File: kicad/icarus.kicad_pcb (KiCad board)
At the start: 4 copper layers, 64.7 x 44.2 mm, 80 parts, among them J1 CAN Bus, J2 CAN Bus, J3 SWD Programming, J4 USB_B_Micro, U1 MAX15062A, U10 XT30, U11 XT30, U12 XT30, U13 LT1787HVIMS8PBF, U14 USBLC6-2SC6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

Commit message: Added gerber and assembly files
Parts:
- added G***: LOGO, icarus_kicad_lib:Icarus_Logo, B.Cu at (147.8, 102.2)
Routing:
- net VSENSE_LOW: vias 0 -> 10
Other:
- board text added: "Jeremy Kanovsky Spring 2021"

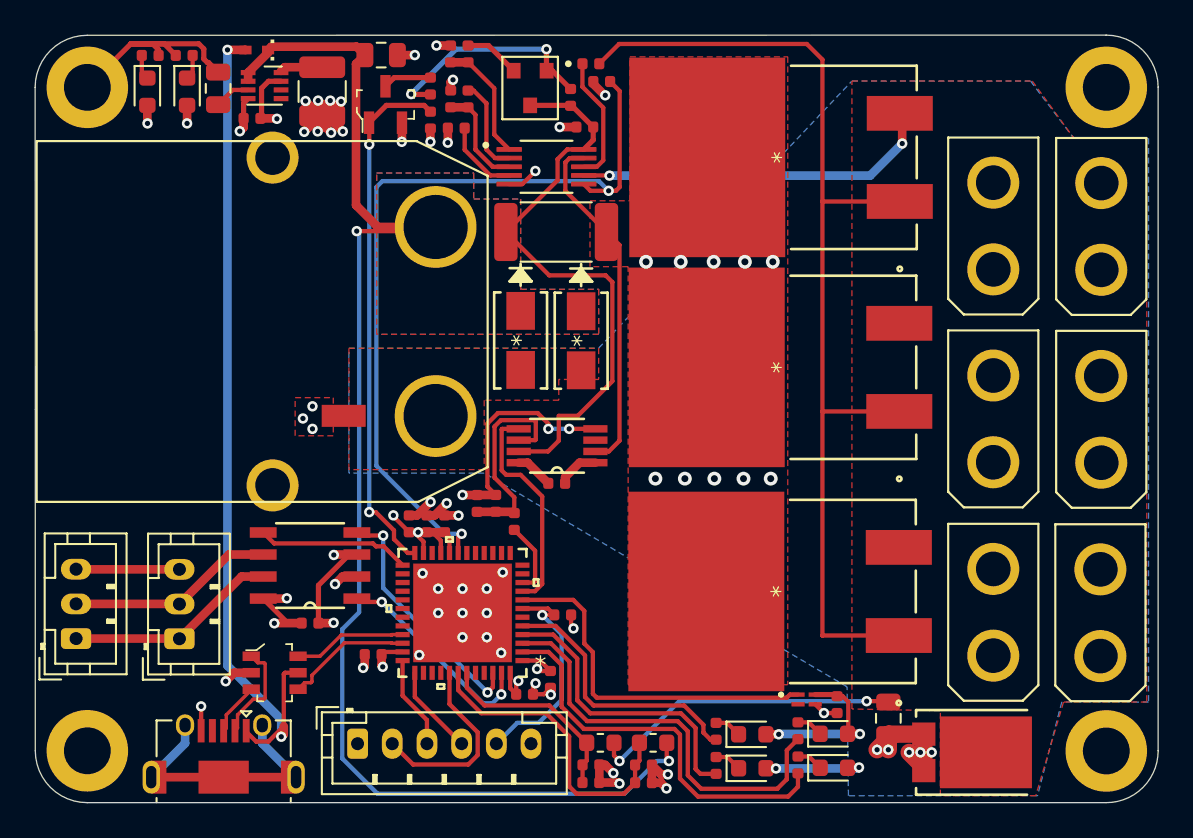
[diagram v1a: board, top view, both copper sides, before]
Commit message: Changed MCU due to sourcing problems
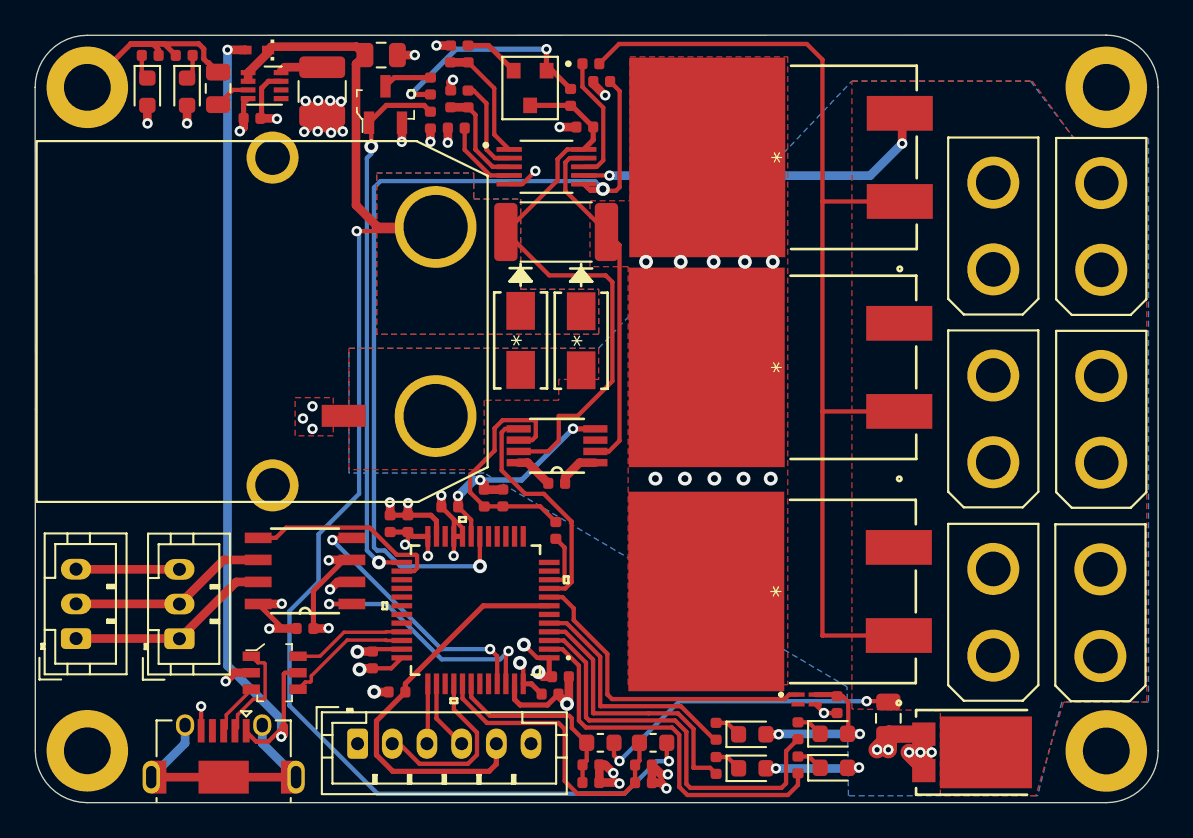
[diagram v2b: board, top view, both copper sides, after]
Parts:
- U2: value STM32G474CEU6 -> STM32G474CET6; footprint icarus_kicad_lib:STM32G474CEU6 -> icarus_kicad_lib:STM32G474CET6
- moved C5 10.5 mm to (133.6, 118.0), turned to 180 degrees
- moved R17 2.45 mm to (142.7, 108.7)
- moved C13 1.47 mm to (142.4, 118.1)
- moved C10 1.10 mm to (134.2, 108.3)
- moved C11 1.10 mm to (133.2, 108.3)
- moved C8 1.02 mm to (136.6, 107.3), turned to 0 degrees
- moved U2 0.77 mm to (138.1, 113.3)
- moved C9 0.60 mm to (143.0, 117.1), turned to 0 degrees
- moved C16 0.51 mm to (139.7, 106.8)
- moved R18 0.51 mm to (138.6, 106.8)
- moved G*** 0.46 mm to (148.0, 101.8)
- moved C1 0.42 mm to (128.3, 114.4)
- moved U3 0.42 mm to (128.3, 111.0)
- moved C12 0.31 mm to (132.2, 116.2), turned to 90 degrees
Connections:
- U2 pad 18: Net-(U2-Pad18) -> PG
- U2 pad 19: PG -> GND
- U2 pad 23: +3V3 -> GND
- U2 pad 24: TPS_ENABLE -> +3V3
- U2 pad 25: CAN_SHDN -> TPS_ENABLE
- U2 pad 26: Net-(U2-Pad26) -> CAN_SHDN
- U2 pad 35: +3V3 -> GND
- U2 pad 36: SWDIO -> +3V3
- U2 pad 37: SWCLK -> SWDIO
- U2 pad 38: Net-(U2-Pad38) -> SWCLK
- U2 pad 40: Net-(U2-Pad40) -> SWO
- U2 pad 41: SWO -> 24V_SENSE
- U2 pad 42: 24V_SENSE -> VSW_SENSE
- U2 pad 43: VSW_SENSE -> Net-(U2-Pad43)
- U2 pad 45: Net-(U2-Pad45) -> CAN_RX
- U2 pad 46: CAN_RX -> CAN_TX
- U2 pad 47: CAN_TX -> GND
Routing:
- net NRST: track 12.8 -> 23.6 mm, vias 1 -> 0
- net PG: track 46.2 -> 52.4 mm
- net GND: track 73.6 -> 79.3 mm, vias 44 -> 30
- net +3V3: track 53.6 -> 58.4 mm, vias 23 -> 26
- net CAN_SHDN: track 8.82 -> 11.7 mm
- net CAN_TX: track 12.3 -> 15.1 mm
- net VSENSE_HIGH: track 112.9 -> 115.5 mm
- net Net-(C16-Pad1): track 12.2 -> 14.5 mm
- net MOSFET_TEMP: track 20.8 -> 18.7 mm
- net SWDIO: track 5.37 -> 3.47 mm
- net LED4: track 15.6 -> 14.1 mm
- net SWCLK: track 5.20 -> 4.05 mm
- net LED3: track 17.3 -> 16.2 mm
- net LED1: track 23.2 -> 22.4 mm
- net SWO: track 11.1 -> 10.2 mm
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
